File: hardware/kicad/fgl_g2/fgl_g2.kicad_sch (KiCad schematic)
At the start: 73 parts, among them J1 USB-C (from bank), J10 XIAO socket 8-14, J2 POT 100k lin + SW, J3 LD2410S socket, J4 LD2410S cable, J5 PORT 1, J6 PORT 2, J7 PORT 3, J8 PORT 4, J9 XIAO socket 1-7, Q1 AO3400A, Q2 AO3401A, U1 XIAO ESP32C3, U2 TPS61500PWPR

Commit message: G2: 90 x 60 mm relayout, horizontal-entry ports, R29 pull-up (D19)
- J5-J8: JILN JL212R-35003B01 push-in blocks (Degson DG212R-THR fits the
  same footprint): wire entry parallel to the board at the top edge, release
  buttons on the wire face. New fgl.pretty footprint and a simplified 3D
  model (tools/make_port_step.py).
- R29 10k pull-up on RADAR_MODE (D8); C16 0402 -> 0603 (C14663).
- Board 74 x 58 -> 90 x 60 mm, laid out with tools/layout_g2b: parts spread
  for rework (min courtyard gap 0.72 mm, median ~1 mm, was 0.3 mm), M3 holes
  in the corners, TP5 clear of the radar, FB routed Kelvin to R21, no via
  within 0.25 mm of any SMD pad.
- ERC 0 errors; netlist 42 nets / 177 connections / 74 parts; DRC 0 errors,
  0 unconnected; verify_pcb 186 pads / 69 footprints. Gerbers, drill, CPL
  (62 placements), BOM, assembly drawing, layout image, 3D render regenerated.
- Firmware comment updated for R29; compile-checked with -Werror.
- Docs: D19, pin tables, ordering, bring-up test G2-T13.

Co-Authored-By: Claude Opus 5.5 <noreply@anthropic.com>
Claude-Session: https://claude.ai/code/session_013HVPKWJHmpHbXpMbmhYHhv
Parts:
- added R29: 10k, Resistor_SMD:R_0603_1608Metric, symbol Device:R_Small
- C16: value 100n 16V -> 100n 50V; footprint Capacitor_SMD:C_0402_1005Metric -> Capacitor_SMD:C_0603_1608Metric; LCSC C1525 -> C14663; MPN CL05B104KO5NNNC -> CC0603KRX7R9BB104; Manufacturer Samsung -> YAGEO
- J5, J6, J7, J8: footprint fgl:TerminalBlock_Degson_DG250-3.5-03P -> fgl:TerminalBlock_JILN_JL212R-3.5-03P_Horizontal; LCSC C7588159 -> C2962951; MPN DG250-3.5-03P-11-00A(H) -> JL212R-35003B01; Manufacturer DEGSON -> JILN
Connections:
- net +3V3: now also R29.1
- net RADAR_MODE: now also R29.2
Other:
- note added: "D4 feeds the XIAO's 5V pin and blocks back-feed from its own USB-C. D6 (GPIO21) is UART0 TX: it toggles during boot, so ISEL goes through R22. D7 (GPIO20, UART0 RX) drives EN. GPIO20 has a ~45 k pull-up at reset, so R18 is 2.2 k: EN stays below 0.4 V until the firmware drives it (also in download mode). D8 (GPIO8) reads JP2, pulled up by R29 (10 k): low = manual mode (radar ignored). Strapping pi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"
- note removed: "D4 feeds the XIAO's 5V pin and blocks back-feed from its own USB-C. D6 (GPIO21) is UART0 TX: it toggles during boot, so ISEL goes through R22. D7 (GPIO20, UART0 RX) drives EN. GPIO20 has a ~45 k pull-up at reset, so R18 is 2.2 k: EN stays below 0.4 V until the firmware drives it (also in download mode). D8 (GPIO8) reads JP2 with its internal pull-up: low = manual mode (radar ignored). Strapping p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"
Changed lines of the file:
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@@
 	(title_block
 		(title "Fused Glass Lighting controller")
-		(date "2026-10-27")
+		(date "2026-10-28")
 		(rev "G2")
 		(company "Rob Lim")
@@
 		)
 	)
-	(text "D4 feeds the XIAO's 5V pin and blocks back-feed from its own USB-C.\nD6 (GPIO21) is UART0 TX: it toggles during boot, so ISEL goes through R22.\nD7 (GPIO20, UART0 RX) drives EN. GPIO20 has a ~45 k pull-up at reset, so R18 is\n2.2 k: EN stays below 0.4 V until the firmware drives it (also in download mode).\nD8 (GPIO8) reads JP2 with its internal pull-up: low = manual mode\n(radar ignored). Strapping pin, but only in download mode: move the\nshunt off 1-2 before forcing download with BOOT. D0/D9 unconnected. J9/J10: 5 mm low-profile sockets\n(JLCPCB fits them); the XIAO's USB-C faces the board edge."
+	(text "D4 feeds the XIAO's 5V pin and blocks back-feed from its own USB-C.\nD6 (GPIO21) is UART0 TX: it toggles during boot, so ISEL goes through R22.\nD7 (GPIO20, UART0 RX) drives EN. GPIO20 has a ~45 k pull-up at reset, so R18 is\n2.2 k: EN stays below 0.4 V until the firmware drives it (also in download mode).\nD8 (GPIO8) reads JP2, pulled up by R29 (10 k): low = manual mode\n(radar ignored). Strapping pin, but only in download mode: move the\nshunt off 1-2 before forcing download with BOOT. D0/D9 unconnected. J9/J10: 5 mm low-profile sockets\n(JLCPCB fits them); the XIAO's USB-C faces the board edge."
 		(exclude_from_sim no)
 		(at 50.8 182.88 0)
@@
 		(at 86.36 157.48)
 	)
+	(symbol
+		(lib_id "Device:R_Small")
+		(at 78.74 132.08 0)
+		(unit 1)
+		(exclude_from_sim no)
+		(in_bom yes)
+		(on_board yes)
+		(dnp no)
+		(property "Reference" "R29"
+			(at 81.28 130.81 0)
+			(effects
+				(font
+					(size 1.27 1.27)
+				)
+				(justify left)
+			)
+		)
+		(property "Value" "10k"
+			(at 81.28 133.35 0)
+			(effects
+				(font
+					(size 1.27 1.27)
+				)
+				(justify left)
+			)
+		)
+		(property "Footprint" "Resistor_SMD:R_0603_1608Metric"
+			(at 78.74 132.08 0)
+			(effects
+				(font
+					(size 1.27 1.27)
+				)
+				(hide yes)
+			)
+		)
+		(property "Datasheet" ""
+			(at 78.74 132.08 0)
+			(effects
+				(font
+					(size 1.27 1.27)
+				)
+				(hide yes)
+			)
+		)
+		(property "Description" ""
+			(at 78.74 132.08 0)
+			(effects
+				(font
+					(size 1.27 1.27)
+				)
+			)
+		)
+		(property "LCSC" "C25804"
+			(at 78.74 132.08 0)
+			(effects
+				(font
+					(size 1.27 1.27)
+				)
+				(hide yes)
+			)
+		)
+		(property "MPN" "0603WAF1002T5E"
+			(at 78.74 132.08 0)
+			(effects
+				(font
+					(size 1.27 1.27)
+				)
+				(hide yes)
+			)
+		)
+		(property "Manufacturer" "UNI-ROYAL"
+			(at 78.74 132.08 0)
+			(effects
+				(font
+					(size 1.27 1.27)
+				)
+				(hide yes)
+			)
+		)
+		(pin "1"
+		)
+		(pin "2"
+		)
+		(instances
+			(project "fgl_g2"
+				(path "/ab8fe160-4d5e-53d4-be1b-69cfad966fcd"
+					(reference "R29")
+					(unit 1)
+				)
+			)
+		)
+	)
+	(symbol
+		(lib_id "power:+3V3")
+		(at 78.74 127 0)
+		(unit 1)
+		(exclude_from_sim no)
+		(in_bom yes)
+		(on_board yes)
+		(dnp no)
+		(property "Reference" "#PWR060"
+			(at 78.74 127 0)
+			(effects
+				(font
+					(size 1.27 1.27)
+				)
+				(hide yes)
+			)
+		)
+		(property "Value" "+3V3"
+			(at 78.74 122.8 0)
+			(effects
+				(font
+					(size 1.27 1.27)
+				)
+			)
+		)
+		(property "Footprint" ""
+			(at 78.74 127 0)
+			(effects
+				(font
+					(size 1.27 1.27)
+				)
+				(hide yes)
+			)
+		)
+		(property "Datasheet" ""
+			(at 78.74 127 0)
+			(effects
+				(font
+					(size 1.27 1.27)
+				)
+				(hide yes)
+			)
+		)
+		(property "Description" ""
+			(at 78.74 127 0)
+			(effects
+				(font
+					(size 1.27 1.27)
+				)
+			)
+		)
+		(pin "1"
+		)
+		(instances
+			(project "fgl_g2"
+				(path "/ab8fe160-4d5e-53d4-be1b-69cfad966fcd"
+					(reference "#PWR060")
+					(unit 1)
+				)
+			)
+		)
+	)
+	(wire
+		(pts
+			(xy 78.74 127) (xy 78.74 129.54)
+		)
+		(stroke
+			(width 0)
+			(type default)
+		)
+	)
+	(wire
+		(pts
+			(xy 78.74 134.62) (xy 78.74 137.16)
+		)
+		(stroke
+			(width 0)
+			(type default)
+		)
+	)
+	(label "RADAR_MODE"
+		(at 78.74 137.16 0)
+		(effects
+			(font
+				(size 1.27 1.27)
+			)
+			(justify left bottom)
+		)
+	)
 	(wire
 		(pts
@@
 		)
 		(property "Value" "RADAR_MODE"
-			(at 104.14 182.88 0)
+			(at 104.14 170.18 0)
 			(effects
 				(font
@@
 					(size 1.27 1.27)
 				)
+				(hide yes)
 			)
 		)
@@
 			)
 		)
-		(property "Value" "100n 16V"
+		(property "Value" "100n 50V"
 			(at 142.24 88.9 0)
 			(effects
@@
 			)
 		)
-		(property "Footprint" "Capacitor_SMD:C_0402_1005Metric"
+		(property "Footprint" "Capacitor_SMD:C_0603_1608Metric"
 			(at 139.7 87.63 0)
 			(effects
@@
 			)
 		)
-		(property "LCSC" "C1525"
+		(property "LCSC" "C14663"
 			(at 139.7 87.63 0)
 			(effects
@@
 			)
 		)
-		(property "MPN" "CL05B104KO5NNNC"
+		(property "MPN" "CC0603KRX7R9BB104"
 			(at 139.7 87.63 0)
 			(effects
@@
 			)
 		)
-		(property "Manufacturer" "Samsung"
+		(property "Manufacturer" "YAGEO"
 			(at 139.7 87.63 0)
 			(effects
@@
 			)
 		)
-		(property "Footprint" "fgl:TerminalBlock_Degson_DG250-3.5-03P"
+		(property "Footprint" "fgl:TerminalBlock_JILN_JL212R-3.5-03P_Horizontal"
 			(at 215.9 157.48 0)
 			(effects
@@
 			)
 		)
-		(property "LCSC" "C7588159"
+		(property "LCSC" "C2962951"
 			(at 215.9 157.48 0)
 			(effects
@@
 			)
 		)
-		(property "MPN" "DG250-3.5-03P-11-00A(H)"
+		(property "MPN" "JL212R-35003B01"
 			(at 215.9 157.48 0)
 			(effects
@@
 			)
 		)
-		(property "Manufacturer" "DEGSON"
+		(property "Manufacturer" "JILN"
 			(at 215.9 157.48 0)
 			(effects
@@
 			)
 		)
-		(property "Footprint" "fgl:TerminalBlock_Degson_DG250-3.5-03P"
+		(property "Footprint" "fgl:TerminalBlock_JILN_JL212R-3.5-03P_Horizontal"
 			(at 276.86 157.48 0)
 			(effects
@@
 			)
 		)
-		(property "LCSC" "C7588159"
+		(property "LCSC" "C2962951"
 			(at 276.86 157.48 0)
 			(effects
@@
 			)
 		)
-		(property "MPN" "DG250-3.5-03P-11-00A(H)"
+		(property "MPN" "JL212R-35003B01"
 			(at 276.86 157.48 0)
 			(effects
@@
 			)
 		)
-		(property "Manufacturer" "DEGSON"
+		(property "Manufacturer" "JILN"
 			(at 276.86 157.48 0)
 			(effects
@@
 			)
 		)
-		(property "Footprint" "fgl:TerminalBlock_Degson_DG250-3.5-03P"
+		(property "Footprint" "fgl:TerminalBlock_JILN_JL212R-3.5-03P_Horizontal"
 			(at 185.42 157.48 0)
 			(effects
@@
 			)
 		)
-		(property "LCSC" "C7588159"
+		(property "LCSC" "C2962951"
 			(at 185.42 157.48 0)
 			(effects
@@
 			)
 		)
-		(property "MPN" "DG250-3.5-03P-11-00A(H)"
+		(property "MPN" "JL212R-35003B01"
 			(at 185.42 157.48 0)
 			(effects
@@
 			)
 		)
-		(property "Manufacturer" "DEGSON"
+		(property "Manufacturer" "JILN"
 			(at 185.42 157.48 0)
 			(effects
@@
 			)
 		)
-		(property "Footprint" "fgl:TerminalBlock_Degson_DG250-3.5-03P"
+		(property "Footprint" "fgl:TerminalBlock_JILN_JL212R-3.5-03P_Horizontal"
 			(at 246.38 157.48 0)
 			(effects
@@
 			)
 		)
-		(property "LCSC" "C7588159"
+		(property "LCSC" "C2962951"
 			(at 246.38 157.48 0)
 			(effects
@@
 			)
 		)
-		(property "MPN" "DG250-3.5-03P-11-00A(H)"
+		(property "MPN" "JL212R-35003B01"
 			(at 246.38 157.48 0)
 			(effects
@@
 			)
 		)
-		(property "Manufacturer" "DEGSON"
+		(property "Manufacturer" "JILN"
 			(at 246.38 157.48 0)
 			(effects

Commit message: G2: datasheet links on every purchased part
Flux flagged parts on generic KiCad symbols as missing a datasheet; no
placed part had its Datasheet field set. set_datasheets.py fills it
(schematic and board) from each part's LCSC number with a direct PDF
link (datasheet.lcsc.com; TI's copy for TPS61500; Seeed wiki for the
XIAO). Test points and mounting holes are left empty.

U1's MPN is now just 113991054 (ordering note moved to Note) and the
shunt's MPN is 2.54, so MPN lookups (Pinscope, Flux) find them.

Nets and footprints unchanged; verify_netlist and verify_pcb pass; ERC
0 errors; DRC same 71 warnings; gerbers identical apart from dates.
Regenerated netlist, schematic PDF, bom.csv, assembly drawing.

Co-Authored-By: Claude Opus 5.5 <noreply@anthropic.com>
Claude-Session: https://claude.ai/code/session_013HVPKWJHmpHbXpMbmhYHhv
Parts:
- U1: MPN 113991054 (order with pre-soldered headers) -> 113991054; Note Plugs into J9/J10; not on the PCB -> Plugs into J9/J10; not on the PCB. Order with pre-soldered 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

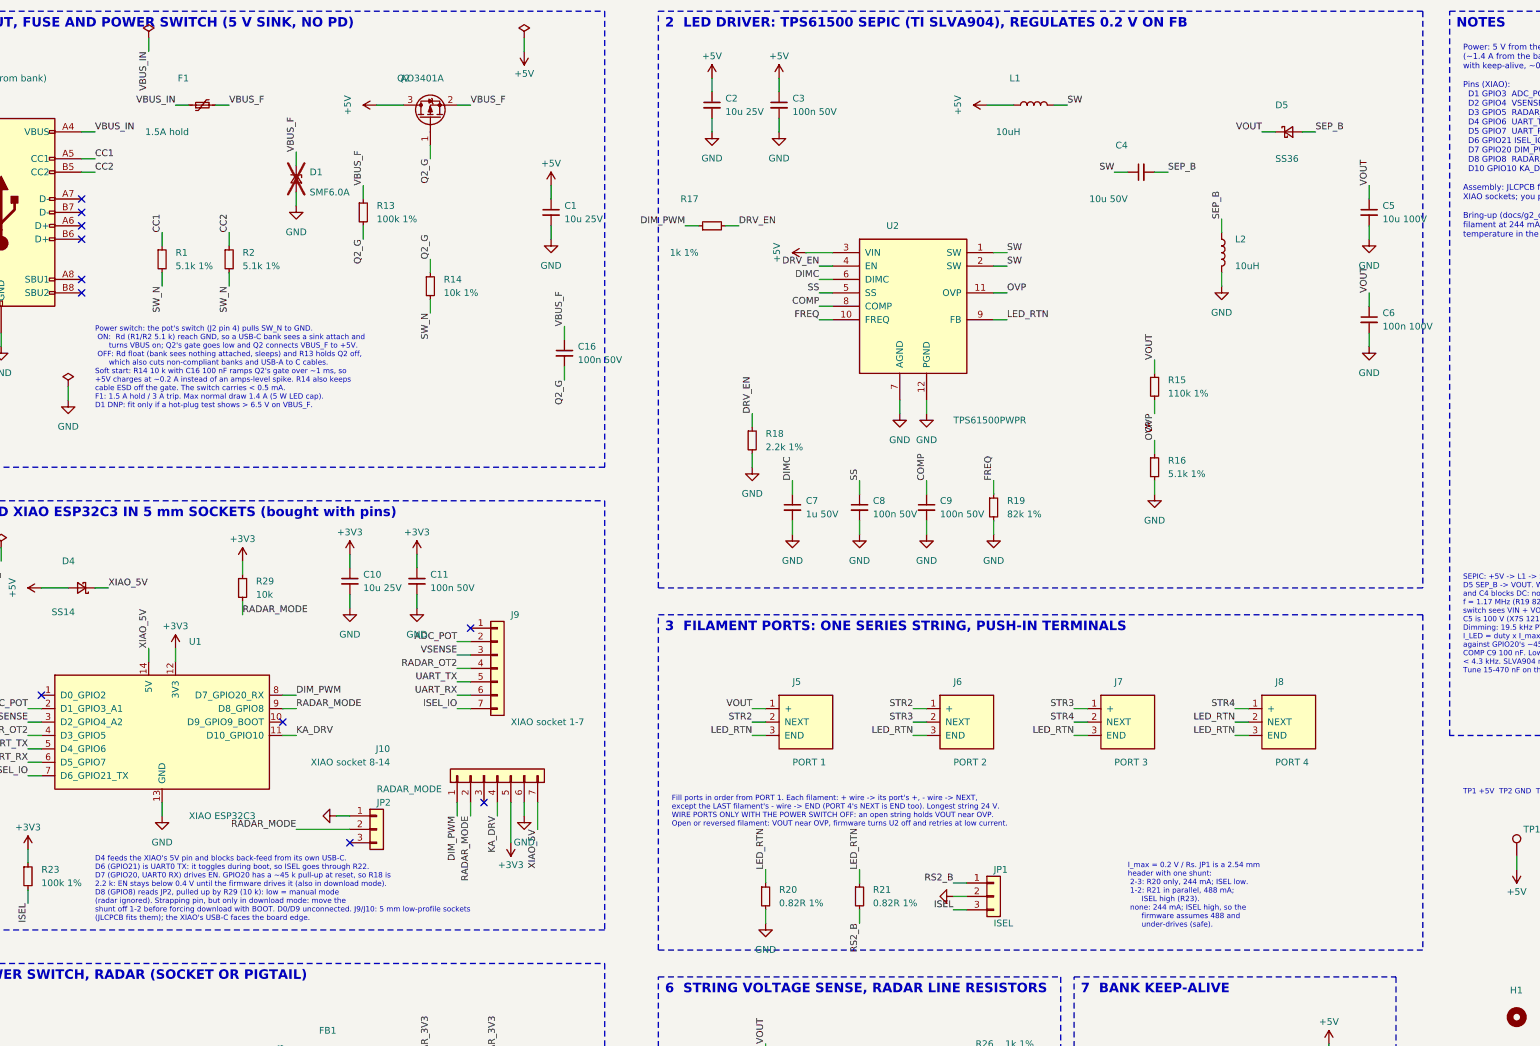
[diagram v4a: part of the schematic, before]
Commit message: G2: act on Flux's schematic review
- Section 2 (SEPIC) redrawn with wires instead of a label on every pin;
  one label per net, labels only where nets leave the section
- Label overlaps cleared: GND at JP1/JP2, VBUS_IN power flag, F1/Q2
  reference and value
- Silkscreen: "Remove shunt to flash" under the JP2 legend (GPIO8 low
  blocks download boot); same instruction in the flashing step
- G2-T6: scope the XIAO 5V pin (limit 6.0 V, XC6210) in both plug
  orientations; D1 cannot hold that, so a failure means an input OVP
  cut-off in G3. G2-T12: try a USB flash with the JP2 shunt on
- docs/g2_flux_schematic_review.md: Flux's findings with resolutions

KiCad netlist identical (nets, names, parts, fields); verify_netlist
passes; ERC 0 errors; DRC same 71 warnings; only F_Silkscreen.gto
changed among the gerbers; position file identical.

Co-Authored-By: Claude Opus 5.5 <noreply@anthropic.com>
Claude-Session: https://claude.ai/code/session_013HVPKWJHmpHbXpMbmhYHhv
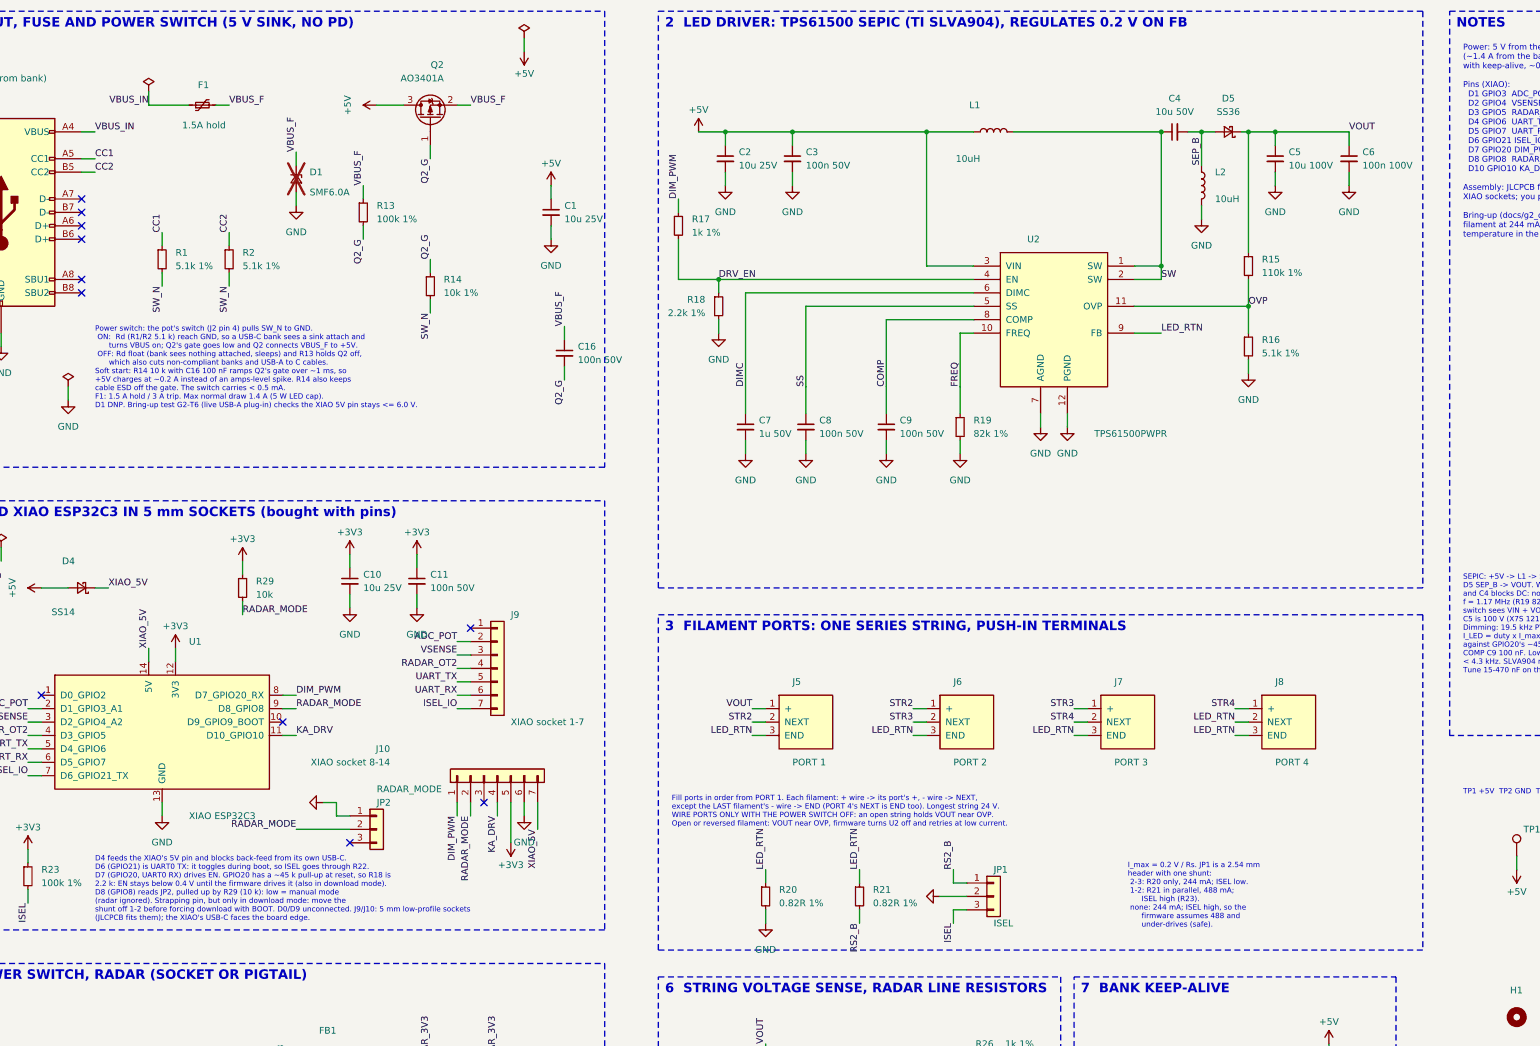
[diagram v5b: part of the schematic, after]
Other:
- moved on the sheet: C2, C3, C4, C5, C6, C7, C8, C9, D5, L1, L2, R15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

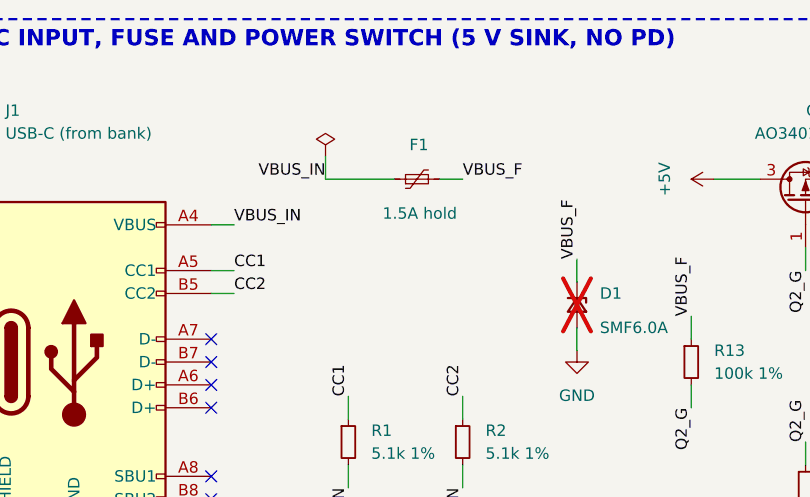
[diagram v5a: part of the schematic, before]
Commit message: G2: fuse to 2 A hold (55 C derating), JLCPCB placement corrections, Flux second pass
F1: SMD1812B150TF/8 (1.06 A hold at 55 C) would trip at the 5 W cap in a
warm frame; now SMD1812B200TF/16 (C269145, ~1.58 A at 55 C), same 1812
footprint. make_cpl.py: every part at its pad-bbox centre (JLCPCB's origin;
KiCad's is pin 1 for headers, sockets, JST, ports, off-centre for the USB-C)
and rotations keyed by LCSC part, checked against JLCPCB's first preview:
J4/J5-J8 +180, JP1/JP2 +270, J1 0, SOT-23 180. Docs: supported strings up to
24 V total, USB-C 1.5 A source for full power, closed-frame G2-T2 run, new
G2-T14 radar through the glass, preview checklist; Flux's second pass saved
with resolutions.

Co-Authored-By: Claude Opus 5.5 <noreply@anthropic.com>
Claude-Session: https://claude.ai/code/session_013HVPKWJHmpHbXpMbmhYHhv
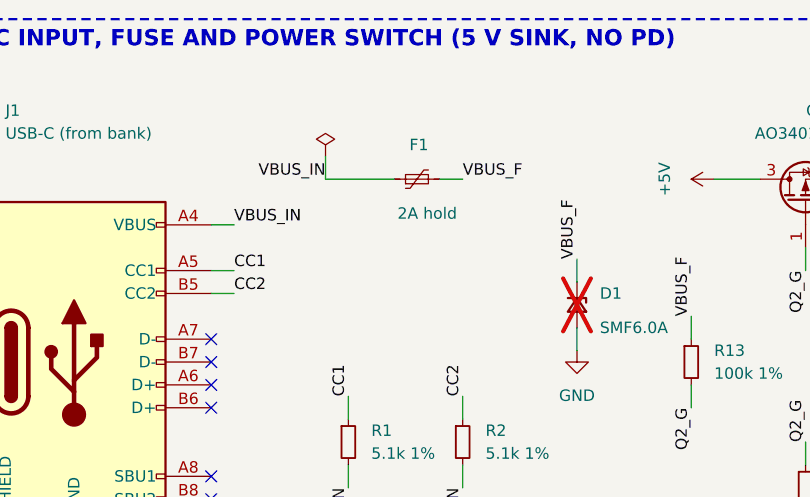
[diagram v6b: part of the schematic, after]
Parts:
- F1: value 1.5A hold -> 2A hold; LCSC C269137 -> C269145; MPN SMD1812B150TF/8 -> SMD1812B200TF/16
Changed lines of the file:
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@@
 			)
 		)
-		(property "Value" "1.5A hold"
+		(property "Value" "2A hold"
 			(at 75.57 44.45 90)
 			(effects
@@
 			)
 		)
-		(property "Datasheet" "https://datasheet.lcsc.com/datasheet/pdf/39c533899a45d694a011d998323027fc.pdf"
+		(property "Datasheet" "https://www.mouser.com/datasheet/2/447/2017100920153415341360-1516460.pdf"
 			(at 71.12 40.64 0)
 			(effects
@@
 			)
 		)
-		(property "LCSC" "C269137"
+		(property "LCSC" "C269145"
 			(at 71.12 40.64 0)
 			(effects
@@
 			)
 		)
-		(property "MPN" "SMD1812B150TF/8"
+		(property "MPN" "SMD1812B200TF/16"
 			(at 71.12 40.64 0)
 			(effects
